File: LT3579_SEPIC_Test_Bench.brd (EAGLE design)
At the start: 74 x 58 mm, 160 parts

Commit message: modiefied baord layout
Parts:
- moved C_LDO_IN_ 11.9 mm to (8.23, 36.6), turned to 180 degrees
- moved 12P_OUTPUT_CONNECTOR1 7.41 mm to (77.1, 31.0)
- moved TP_LDO_OUT_ 4.94 mm to (7.55, 50.1), turned to 180 degrees
- moved 4P_INPUT_CONNECTOR1 3.76 mm to (5.25, 9.33), turned to 0 degrees
- moved PMOS_REVERSE_V_PROTECTION 3.17 mm to (8.40, 19.9), turned to 270 degrees
- moved LDO_ 1.92 mm to (7.90, 42.4), turned to 90 degrees
- moved C_OUT_2_1 1.78 mm to (57.4, 34.0)
- moved C_OUT_3_1 1.78 mm to (60.1, 34.0)
- moved R_LED_10K_1 1.78 mm to (62.4, 34.4)
- moved C_OUT_1_1 1.78 mm to (54.8, 34.0)
- moved C_DECOUPLE_CH_GND_1 0.91 mm to (8.01, 34.5)
- moved R_10K_FILTER_ 0.89 mm to (52.5, 48.5)
- moved TP_CF_1 0.85 mm to (38.7, 30.4)
- moved C_DECOUPLE_CH_GND_2 0.81 mm to (5.31, 29.4)
- moved D1_1 0.80 mm to (31.7, 26.7)
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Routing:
- net VIN: track 0.00 -> 212.9 mm, vias 0 -> 3
- net VOUT_: track 0.00 -> 52.2 mm, vias 0 -> 1
- net SW1-2_2: track 0.00 -> 50.9 mm
- net SW1-2_1: track 0.00 -> 49.5 mm
- net SW1-2_: track 0.00 -> 44.1 mm
- net VOUT_2: track 0.00 -> 41.2 mm, vias 0 -> 1
- net VOUT_1: track 0.00 -> 32.3 mm, vias 0 -> 1
- net N$3: track 0.00 -> 26.5 mm, vias 0 -> 1
- net N$7: track 0.00 -> 25.3 mm, vias 0 -> 1
- net N$13: track 0.00 -> 24.6 mm, vias 0 -> 1
- net N$1: track 0.00 -> 24.1 mm, vias 0 -> 2
- net N$5: track 0.00 -> 24.1 mm, vias 0 -> 2
- net N$9: track 0.00 -> 21.5 mm, vias 0 -> 2
- net GATE_: track 0.00 -> 13.6 mm, vias 0 -> 1
- net GATE_2: track 0.00 -> 13.5 mm, vias 0 -> 1
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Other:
- board size 74 x 58 mm -> 83.8 x 62.2 mm

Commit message: modified layout
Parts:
- moved TP_FAULT_LS_1 3.28 mm to (33.0, 26.6), turned to 180 degrees
- moved TP_FAULT_LS_ 3.19 mm to (32.0, 47.5), turned to 0 degrees
- moved TP_FAULT_LS_2 3.10 mm to (33.5, 5.95), turned to 180 degrees
- moved TP_CH_GND_1 1.33 mm to (21.0, 30.7)
- moved TP_CH_GND_2 1.33 mm to (21.0, 10.2)
- moved R_SHUNT_GND_1 1.20 mm to (23.2, 34.6)
- moved TP_GND_2 1.16 mm to (25.5, 10.2)
- moved R_SHUNT_GND_2 1.11 mm to (23.2, 14.4)
- moved TP_GND_1 1.04 mm to (25.5, 30.6)
- moved C_LS_2 0.70 mm to (35.0, 3.32)
- moved R_LS_DRAIN_2 0.70 mm to (33.2, 3.55)
- moved TP_RT_ 0.30 mm to (57.5, 51.2)
- moved R_SHUNT_GND_ 0.06 mm to (23.2, 54.2)
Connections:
- removed net 0: C_68N_FILTER_.2, C_68N_FILTER_1.2, C_68N_FILTER_2.2, C_C_.2, C_C_1.2, C_C_2.2, C_F_.2, C_F_1.2, C_F_2.2, C_IN_1_.2, C_IN_1_1.2, C_IN_1_2.2, C_IN_2_.2, C_IN_2_1.2, C_IN_2_2.2, C_LDO_IN_.2, C_LDO_OUT_.2, C_LS_.2, C_LS_1.2, C_LS_2.2, C_OUT_1_.2, C_OUT_1_1.2, C_OUT_1_2.2, C_OUT_2_.2, C_OUT_2_1.2, C_OUT_2_2.2, C_OUT_3_.2, C_OUT_3_1.2, C_OUT_3_2.2, C_SS_.2, C_SS_1.2, C_SS_2.2, L1L2_.4, L1L2_1.4, L1L2_2.4, LED_.2, LED_1.2, LED_2.2, LT3579_IC_.21, LT3579_IC_1.21, LT3579_IC_2.21, NMOS_LDO_.2, NMOS_LDO_1.2, NMOS_LDO_2.2, PMOS_REVERSE_V_PROTECTION.4, R_5K_FILTER_\.2, R_5K_FILTER_\1.2, R_5K_FILTER_\2.2, R_T_.2, R_T_1.2, R_T_2.2, R_UVLO2_.1, R_UVLO2_1.1, R_UVLO2_2.1, TP_GND1_.1, TP_GND1_1.1, TP_GND1_2.1, TP_GND2_.1, TP_GND2_1.1, TP_GND2_2.1, TP_GND3_.1, TP_GND3_1.1, TP_GND3_2.1, TP_GND4_.1, TP_GND4_1.1, TP_GND4_2.1
- net CH_GND: now also PMOS_REVERSE_V_PROTECTION.4
- net GND: now also C_68N_FILTER_.2, C_68N_FILTER_1.2, C_68N_FILTER_2.2, C_C_.2, C_C_1.2, C_C_2.2, C_F_.2, C_F_1.2, C_F_2.2, C_IN_1_.2, C_IN_1_1.2, C_IN_1_2.2, C_IN_2_.2, C_IN_2_1.2, C_IN_2_2.2, C_LDO_IN_.2, C_LDO_OUT_.2, C_LS_.2, C_LS_1.2, C_LS_2.2, C_OUT_1_.2, C_OUT_1_1.2, C_OUT_1_2.2, C_OUT_2_.2, C_OUT_2_1.2, C_OUT_2_2.2, C_OUT_3_.2, C_OUT_3_1.2, C_OUT_3_2.2, C_SS_.2, C_SS_1.2, C_SS_2.2, L1L2_.4, L1L2_1.4, L1L2_2.4, LED_.2, LED_1.2, LED_2.2, LT3579_IC_.21, LT3579_IC_1.21, LT3579_IC_2.21, NMOS_LDO_.2, NMOS_LDO_1.2, NMOS_LDO_2.2, R_5K_FILTER_\.2, R_5K_FILTER_\1.2, R_5K_FILTER_\2.2, R_T_.2, R_T_1.2, R_T_2.2, R_UVLO2_.1, R_UVLO2_1.1, R_UVLO2_2.1, TP_GND1_.1, TP_GND1_1.1, TP_GND1_2.1, TP_GND2_.1, TP_GND2_1.1, TP_GND2_2.1, TP_GND3_.1, TP_GND3_1.1, TP_GND3_2.1, TP_GND4_.1, TP_GND4_1.1, TP_GND4_2.1
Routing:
- net LDO_OUT_: track 10.4 -> 90.6 mm, vias 0 -> 4
- net FAULT_LS_OUT_2: track 10.8 -> 65.0 mm, vias 0 -> 2
- net CLK_FILTER_OUT_2: track 10.1 -> 63.2 mm, vias 0 -> 2
- net FAULT_LS_OUT_: track 9.33 -> 52.5 mm, vias 0 -> 2
- net FAULT_LS_OUT_1: track 10.4 -> 49.6 mm, vias 0 -> 2
- net CLK_FILTER_OUT_: track 9.14 -> 47.0 mm, vias 0 -> 2
- net CLK_FILTER_OUT_1: track 8.99 -> 41.0 mm, vias 0 -> 2
- net VC_: track 0.00 -> 17.2 mm, vias 0 -> 2
- net VC_1: track 0.00 -> 16.8 mm, vias 0 -> 2
- net VC_2: track 0.00 -> 15.4 mm, vias 0 -> 2
- net SW1-2_2: track 50.9 -> 36.2 mm
- net SW1-2_: track 44.1 -> 29.9 mm
- net SW1-2_1: track 49.5 -> 38.9 mm
- net VIN_CONNECTOR: track 9.97 -> 0.00 mm
- net FAULT_2: track 4.41 -> 10.6 mm
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- added copper zone on layer 1, net CH_GND
- added copper zone on layer 16, net CH_GND
- added copper zone on layer 1, net GND
- added copper zone on layer 16, net GND
- added copper zone on layer 2, net GND
- added copper zone on layer 1, net SW1-2_
- added copper zone on layer 1, net SW1-2_1
- added copper zone on layer 1, net SW1-2_2
- added copper zone on layer 1, net VIN
- added copper zone on layer 1, net VIN_CONNECTOR
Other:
- board size 83.8 x 62.2 mm -> 84.9 x 63.2 mm

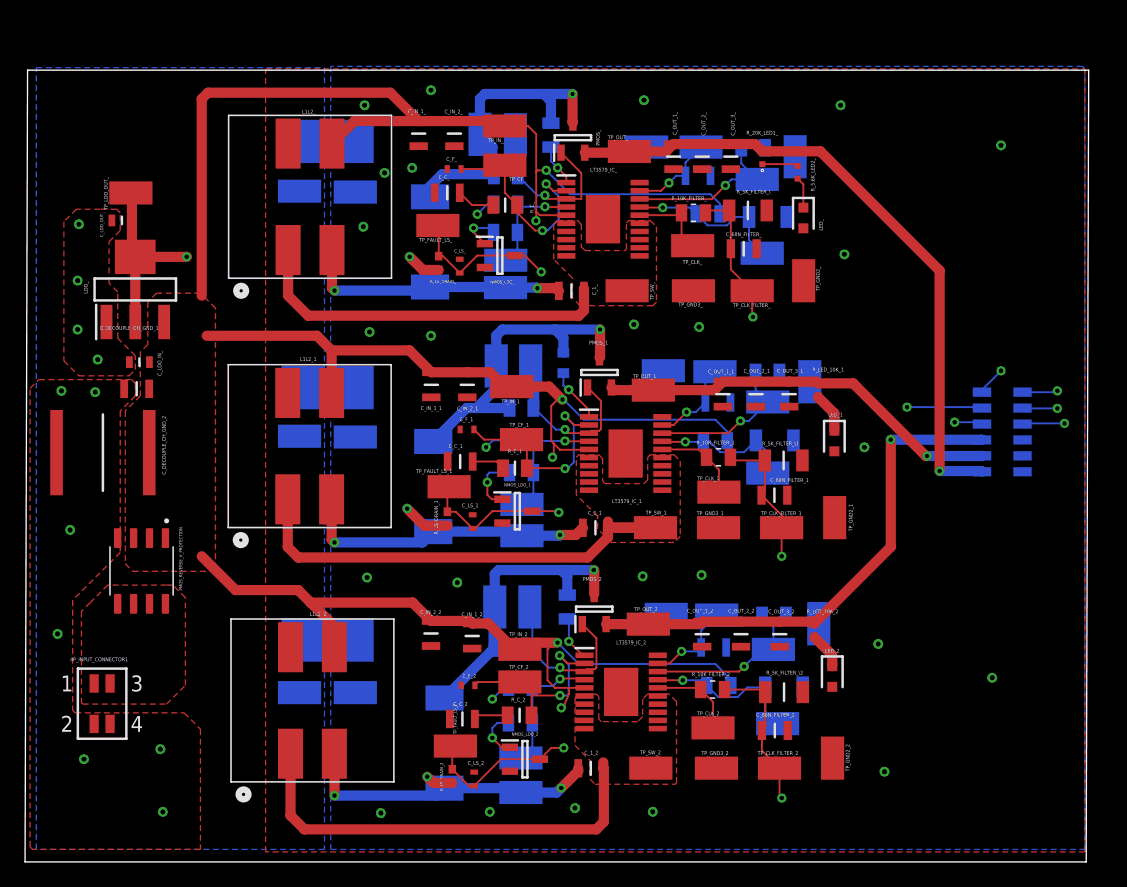
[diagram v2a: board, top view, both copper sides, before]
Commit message: finished board routing
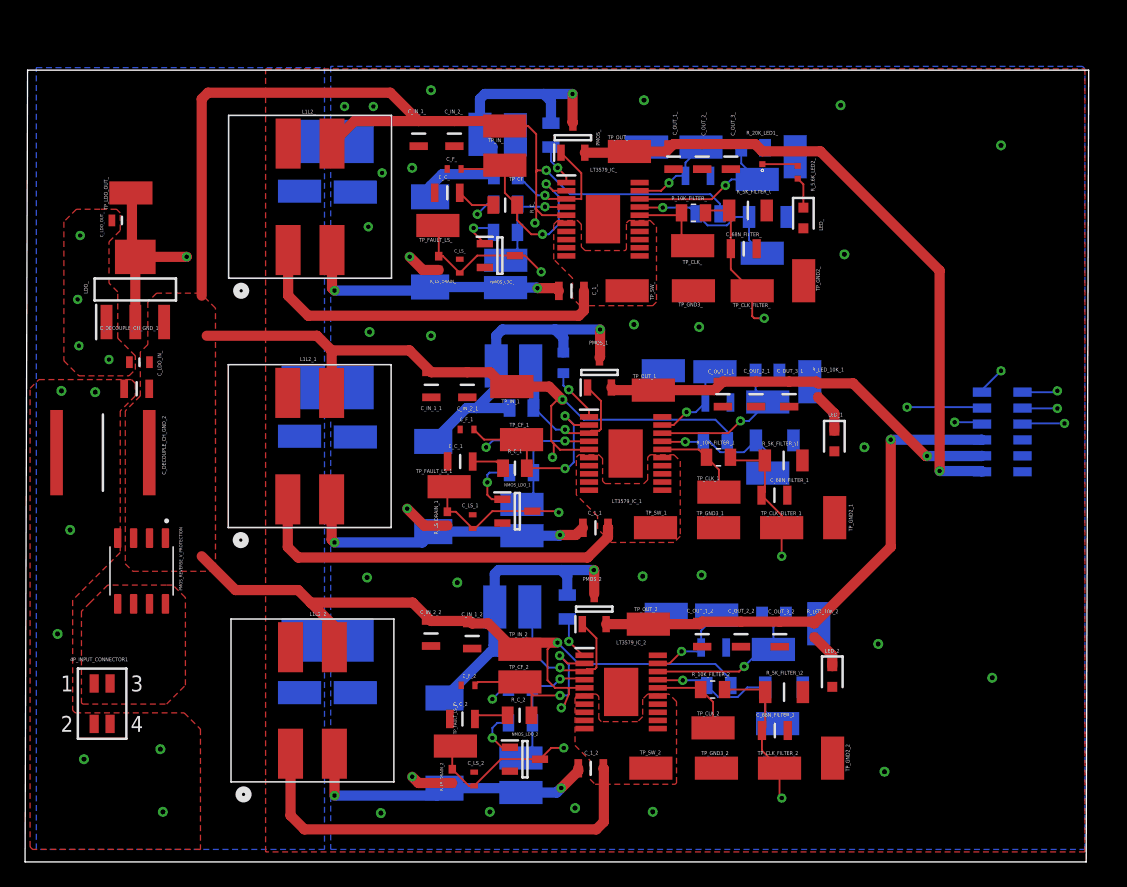
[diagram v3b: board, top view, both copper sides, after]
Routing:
- net SW1-2_1: track 38.9 -> 31.1 mm
- net SW1-2_2: track 36.2 -> 35.0 mm
- net VC_: track 17.2 -> 18.0 mm
- net LDO_OUT_: track 90.6 -> 91.3 mm

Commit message: modified routing
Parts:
- moved C_LS_ 3.42 mm to (34.7, 47.6)
- moved C_OUT_1_1 3.42 mm to (55.7, 37.3)
- moved TP_SHDN_ 3.42 mm to (58.8, 48.6)
- moved TP_SW_ 3.42 mm to (48.1, 45.6)
- moved C_DECOUPLE_CH_GND_1 3.42 mm to (8.91, 37.8)
- moved C_LDO_OUT_ 3.42 mm to (7.73, 51.2)
- moved C_68N_FILTER_ 3.42 mm to (57.4, 49.0)
- moved C_F_ 3.42 mm to (34.2, 55.3)
- moved C_F_1 3.42 mm to (35.3, 34.5)
- moved C_IN_1_1 3.42 mm to (32.4, 38.1)
- moved C_IN_2_1 3.42 mm to (35.3, 38.1)
- moved C_OUT_2_1 3.42 mm to (58.3, 37.3)
- moved C_OUT_3_1 3.42 mm to (61.0, 37.3)
- moved C_SS_1 3.42 mm to (55.3, 36.7)
- moved D1_ 3.42 mm to (32.3, 49.5)
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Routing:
- net VIN: track 219.3 -> 216.7 mm
- net SW1-2_1: track 31.1 -> 30.4 mm
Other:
- board size 84.9 x 63.2 mm -> 85 x 62.1 mm

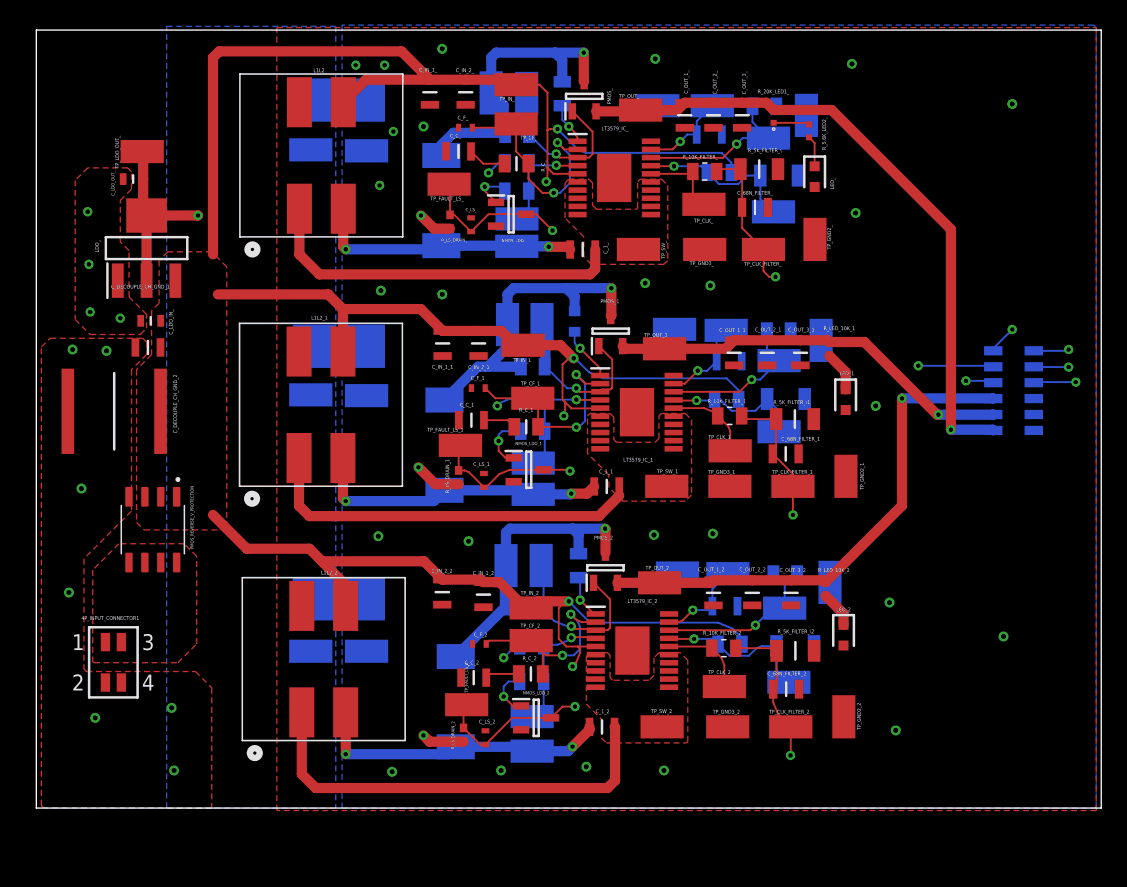
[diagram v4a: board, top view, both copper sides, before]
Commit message: modified traces to be curved.
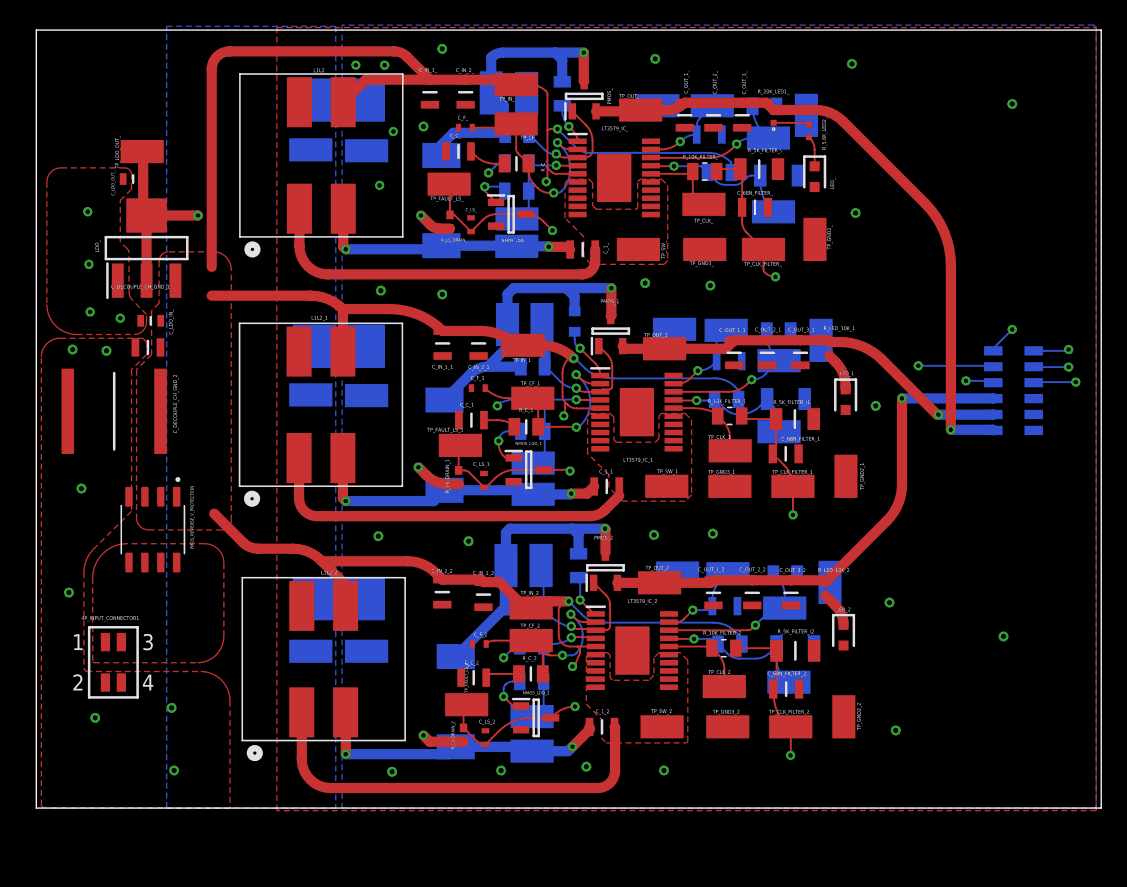
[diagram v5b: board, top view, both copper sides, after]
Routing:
- net VIN: track 216.7 -> 214.9 mm
- net SW1-2_2: track 34.9 -> 33.8 mm
- net LDO_OUT_: track 91.3 -> 90.2 mm
- net SW1-2_: track 29.7 -> 28.9 mm
- net CLK_FILTER_OUT_: track 46.8 -> 46.1 mm
- net VOUT_: track 52.2 -> 51.4 mm
- net FAULT_LS_OUT_: track 52.5 -> 51.8 mm
- net VC_: track 18.0 -> 17.4 mm
- net FAULT_LS_OUT_2: track 65.0 -> 64.4 mm

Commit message: Modified Text Sizes of Test Points, Addeed more GND Vias, Added Mounting Holes
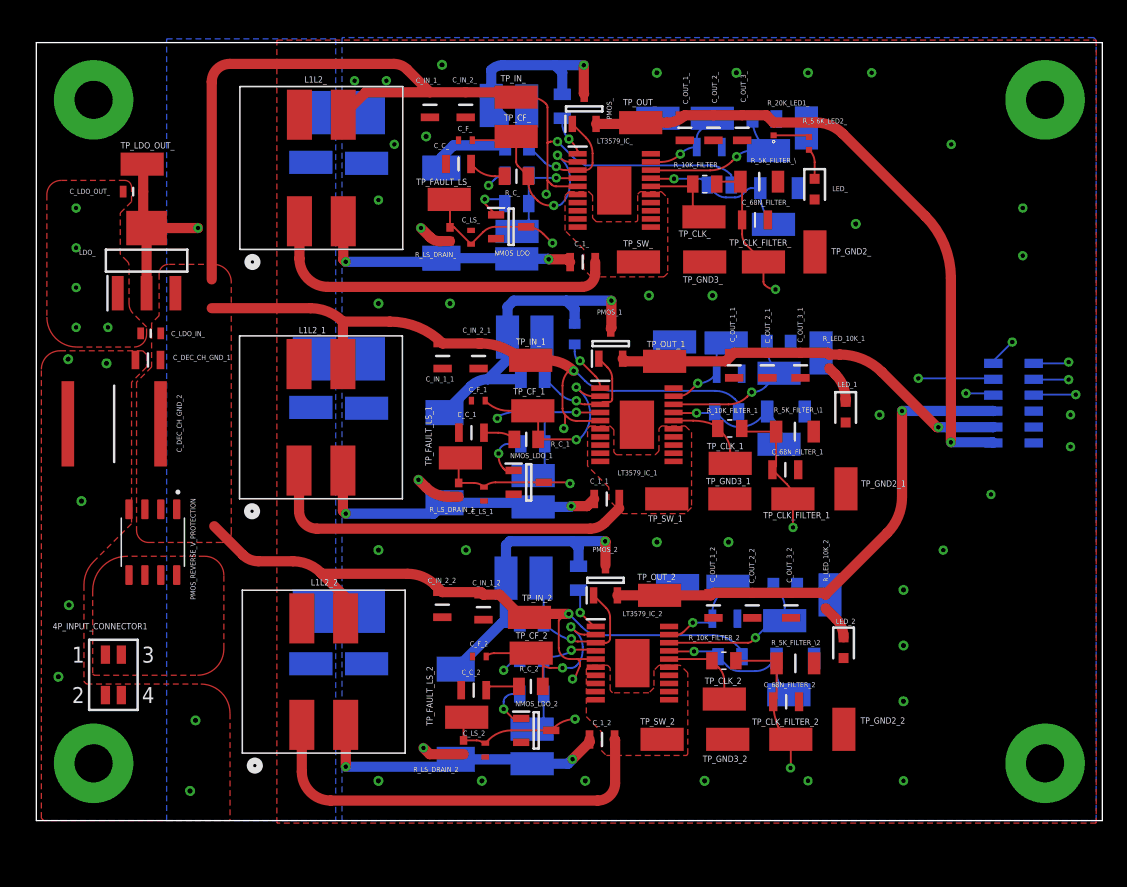
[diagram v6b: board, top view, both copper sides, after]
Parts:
- removed C_DECOUPLE_CH_GND_1: CGA4F4C0G2W222J085AE, SamacSys_Parts:CAPC2012X100N
- removed C_DECOUPLE_CH_GND_2: CGADN3X7R1E476M230LE, SamacSys_Parts:CAPC7563X250N
- added C_DEC_CH_GND_1: CGA4F4C0G2W222J085AE, SamacSys_Parts:CAPC2012X100N
- added C_DEC_CH_GND_2: CGADN3X7R1E476M230LE, SamacSys_Parts:CAPC7563X250N
- added U$1, U$2, U$3, U$4: THROUGH_HOLE_, THROUGH_HOLE:THROUGH_HOLE
- moved TP_IN_1 1.34 mm to (39.5, 36.7)
- moved C_68N_FILTER_1 1.27 mm to (59.8, 28.0)
- moved TP_FAULT_LS_ 1.22 mm to (33.0, 49.6)
- moved C_LS_1 1.09 mm to (35.7, 26.1), turned to 270 degrees
- moved R_GATE_2 1.00 mm to (39.5, 15.8)
- moved TP_FAULT_2 1.00 mm to (39.6, 7.30)
- moved 12P_OUTPUT_CONNECTOR1 1.00 mm to (78.0, 33.3)
- moved 4P_INPUT_CONNECTOR1 1.00 mm to (6.15, 11.6)
- moved C_1_ 1.00 mm to (43.6, 44.6)
- moved C_1_1 1.00 mm to (45.5, 25.7)
- moved C_1_2 1.00 mm to (45.2, 6.47)
- moved C_68N_FILTER_ 1.00 mm to (57.4, 48.0)
- moved C_68N_FILTER_2 1.00 mm to (59.9, 9.49)
- moved C_C_ 1.00 mm to (33.7, 52.4)
- moved C_C_1 1.00 mm to (34.7, 31.0)
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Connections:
- net CH_GND: now also C_DEC_CH_GND_1.1, C_DEC_CH_GND_2.1; no longer C_DECOUPLE_CH_GND_1.1, C_DECOUPLE_CH_GND_2.1
- net VIN: now also C_DEC_CH_GND_1.2, C_DEC_CH_GND_2.2; no longer C_DECOUPLE_CH_GND_1.2, C_DECOUPLE_CH_GND_2.2
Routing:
- net FAULT_LS_OUT_2: track 64.4 -> 63.6 mm
- net FAULT_LS_OUT_1: track 49.1 -> 48.3 mm
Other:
- board size 85 x 62.1 mm -> 85.1 x 62.1 mm
